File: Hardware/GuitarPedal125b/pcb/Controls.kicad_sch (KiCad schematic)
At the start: 19 parts

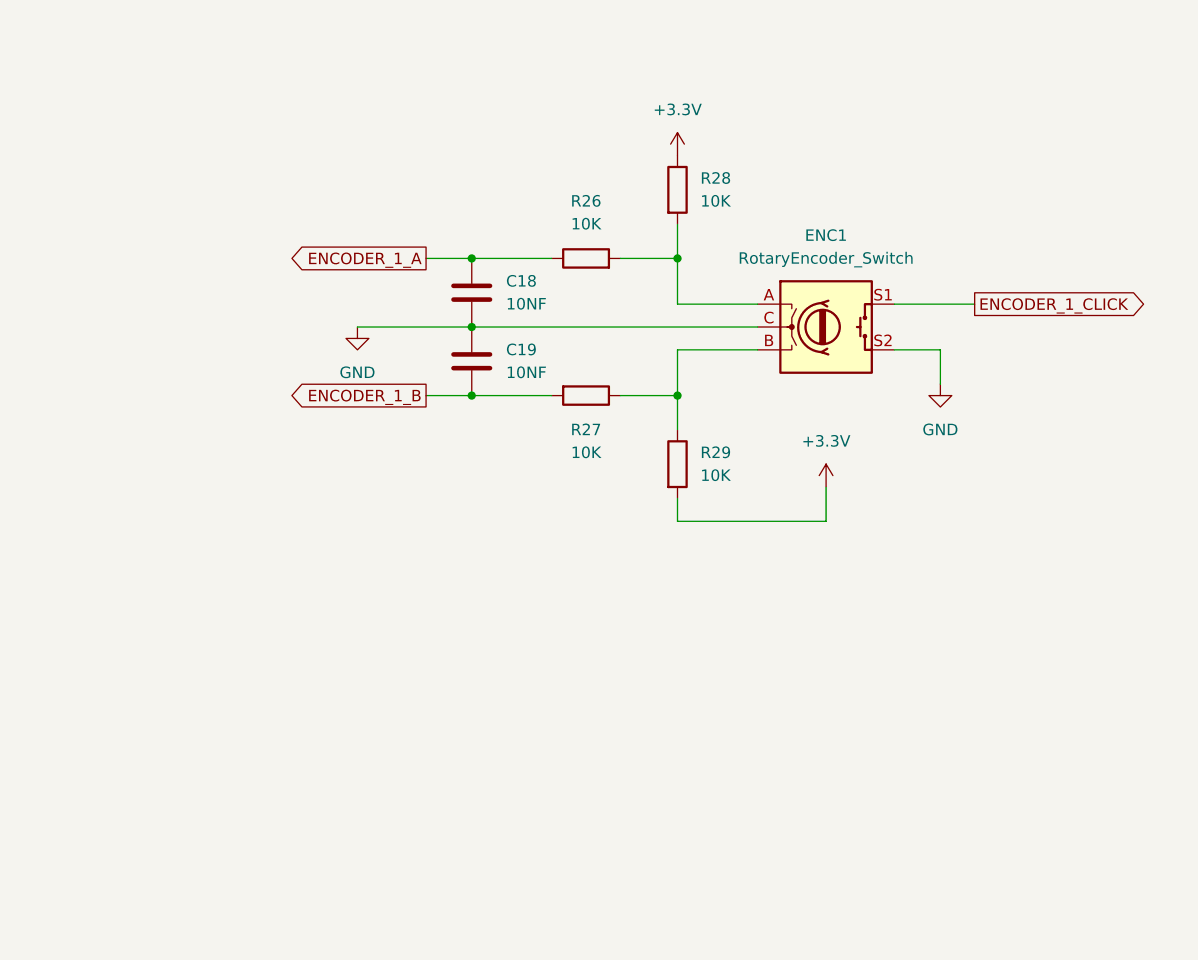
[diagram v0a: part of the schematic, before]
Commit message: Replace screen and encoder by 3 toggle switches and SD card reader.
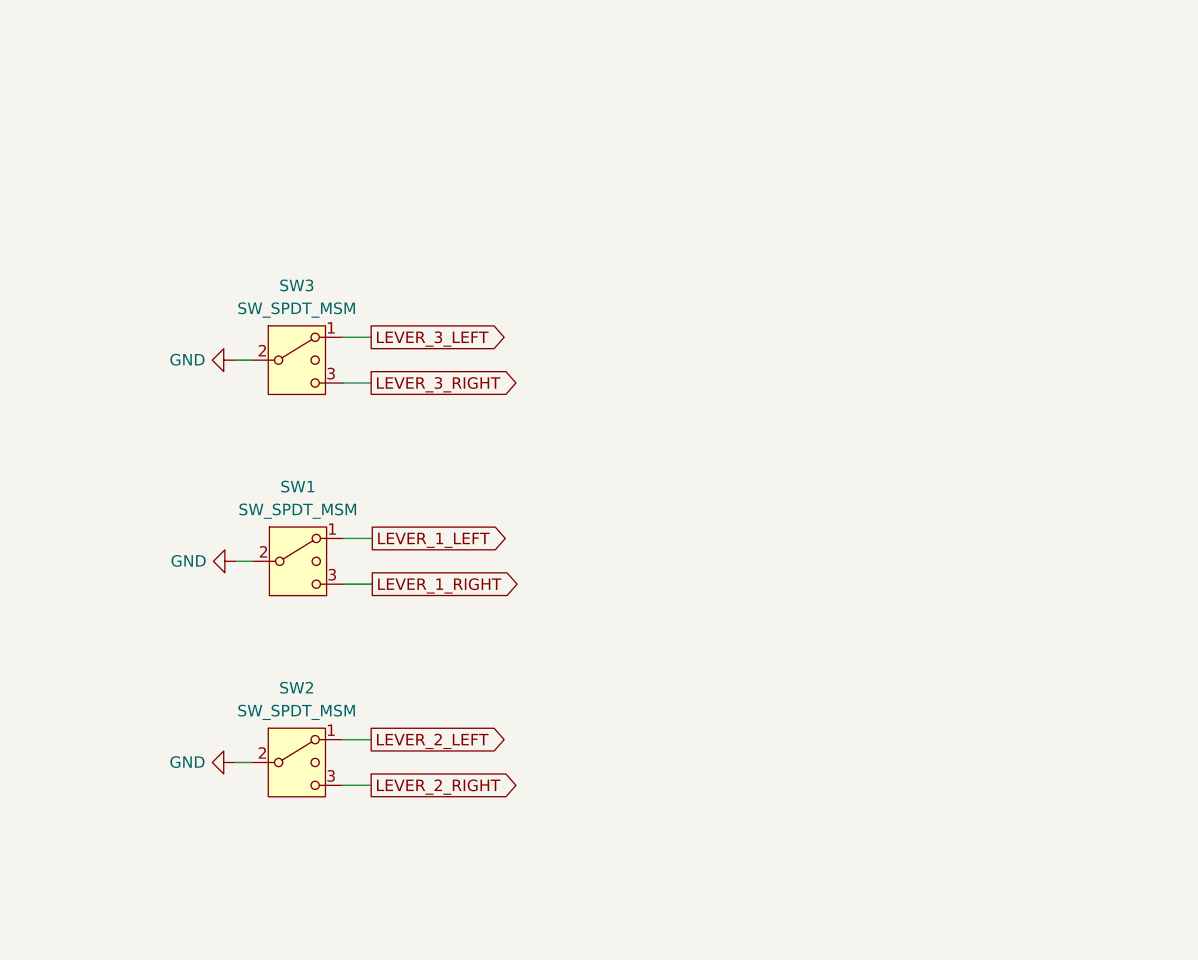
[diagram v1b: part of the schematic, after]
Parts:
- removed C18, C19: 10NF, Capacitor_SMD:C_0805_2012Metric, symbol Device:C
- removed ENC1: RotaryEncoder_Switch, Rotary_Encoder:RotaryEncoder_Alps_EC11E-Switch_Vertical_H20mm, symbol Device:RotaryEncoder_Switch
- removed R26, R27, R28, R29: 10K, Resistor_SMD:R_0805_2012Metric, symbol Device:R
- added SW1, SW2, SW3: SW_SPDT_MSM, MyFootprints:MTS-103, symbol Switch:SW_SPDT_MSM
- FS1, FS2, LED1, LED2, POT1, POT2, POT3, POT4, POT5, POT6: now left out of the parts list
- R24, R25: MPN (none) -> C17513
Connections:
- net GND: now also SW1.2 (3), SW2.2 (3), SW3.2 (3)
- new net LEVER_1_LEFT: SW1.1
- new net LEVER_1_RIGHT: SW1.3 (4)
- new net LEVER_2_LEFT: SW2.1
- new net LEVER_2_RIGHT: SW2.3 (4)
- new net LEVER_3_LEFT: SW3.1
- new net LEVER_3_RIGHT: SW3.3 (4)
